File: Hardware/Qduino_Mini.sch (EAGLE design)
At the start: 44 parts, among them Q1 PFET, U1 ATMEGA32U41:1-LESS_PASTE, U2 MCP73831, U3 MAX17048, U4 TPS78233, U7 DNP, Y1 8MHZ

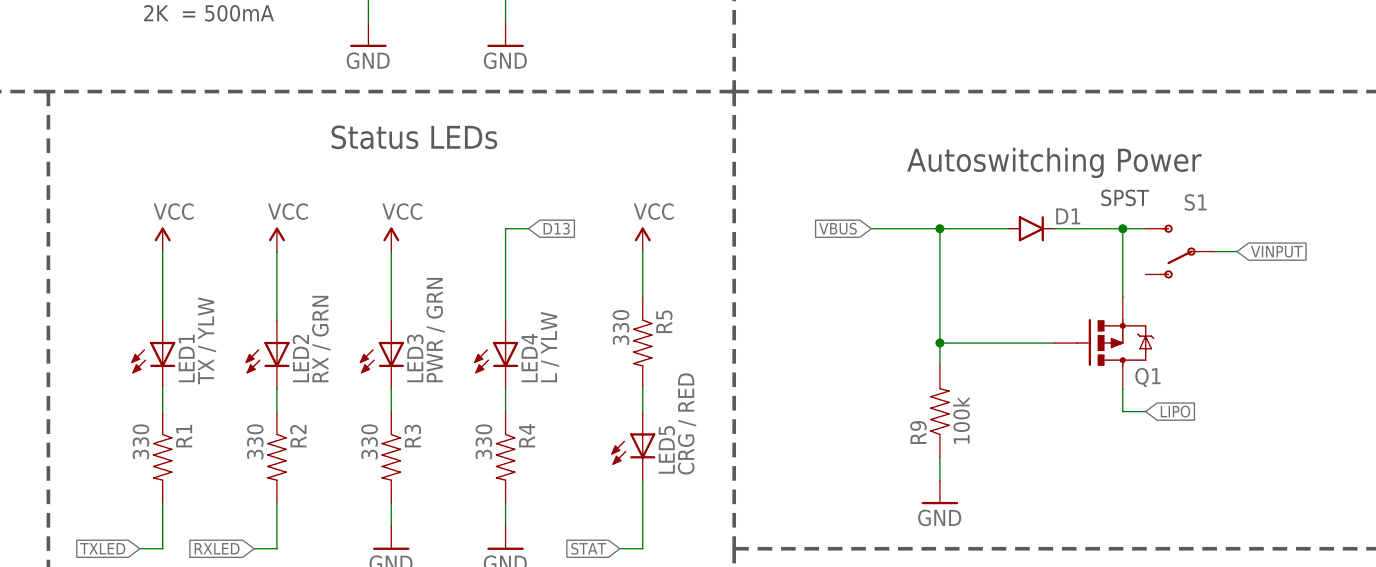
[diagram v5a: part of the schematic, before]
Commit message: Fixed library caused(?) inconsistencies
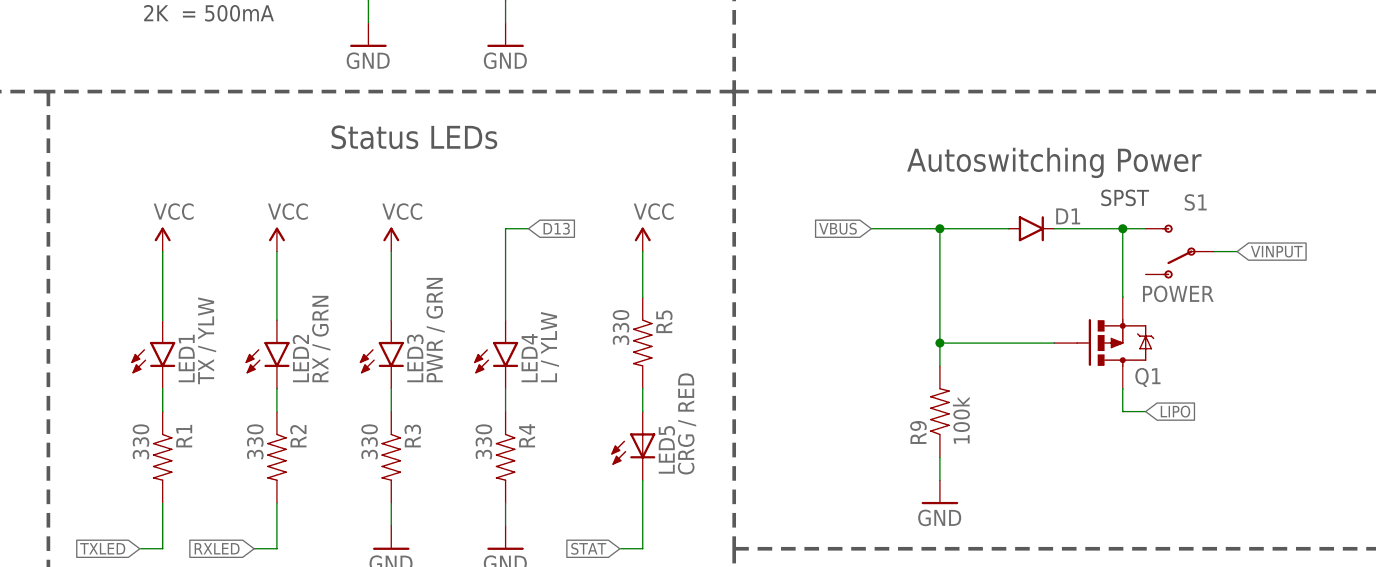
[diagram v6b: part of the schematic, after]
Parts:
- removed U$1: MIGHTYQ-S-SILK, Qtechknow:MIGHTYQ-S-SILK
- removed U$5: MIGHTYQ-L-SILK, Qtechknow:MIGHTYQ-L-SILK
- removed U$7, U$8, U$9: QHEADERS, Qtechknow:QHEADERS
- added U5: MIGHTYQ-L-SILK, SparkFun-Aesthetics:MIGHTYQ-L-SILK
- added U6: MIGHTYQ-S-SILK, SparkFun-Aesthetics:MIGHTYQ-S-SILK
- D1: value (none) -> BAS16JTR
- LED1, LED4: device SFE LED:LED0603 -> SparkFun-LED:LED-YELLOW0603
- LED2, LED3: device SFE LED:LED0603 -> SparkFun-LED:LED-GREEN0603
- S1: value (none) -> POWER
- U4: device Pinoccio:LDO-TPS78233 -> SparkFun-PowerIC:LDO-TPS78233
- U7: device Qduino_Mini:QDUINOMINI -> SparkFun-Aesthetics:QDUINOMINI
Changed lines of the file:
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@@
 <part name="GND2" library="SFE Aesthetics" deviceset="GND" device=""/>
 <part name="GND3" library="SFE Aesthetics" deviceset="GND" device=""/>
-<part name="LED1" library="SFE LED" deviceset="LED" device="0603" value="TX / YLW">
+<part name="LED1" library="SparkFun-LED" deviceset="LED-YELLOW" device="0603" value="TX / YLW">
 <attribute name="PROD_ID" value="DIO-09003"/>
 </part>
-<part name="LED2" library="SFE LED" deviceset="LED" device="0603" value="RX / GRN">
+<part name="LED2" library="SparkFun-LED" deviceset="LED-GREEN" device="0603" value="RX / GRN">
 <attribute name="PROD_ID" value="DIO-00821"/>
 </part>
 <part name="P+3" library="SFE Aesthetics" deviceset="VCC" device=""/>
-<part name="LED3" library="SFE LED" deviceset="LED" device="0603" value="PWR / GRN">
+<part name="LED3" library="SparkFun-LED" deviceset="LED-GREEN" device="0603" value="PWR / GRN">
 <attribute name="PROD_ID" value="DIO-00821"/>
 </part>
 <part name="P+4" library="SFE Aesthetics" deviceset="VCC" device=""/>
 <part name="GND6" library="SFE Aesthetics" deviceset="GND" device=""/>
-<part name="LED4" library="SFE LED" deviceset="LED" device="0603" value="L / YLW">
+<part name="LED4" library="SparkFun-LED" deviceset="LED-YELLOW" device="0603" value="L / YLW">
 <attribute name="PROD_ID" value="DIO-09003"/>
 </part>
@@
 <attribute name="PROD_ID" value="CAP-00868"/>
 </part>
-<part name="S1" library="SparkFun-Electromechanical" deviceset="SWITCH-SPDT" device="-SMD-A">
+<part name="S1" library="SparkFun-Electromechanical" deviceset="SWITCH-SPDT" device="-SMD-A" value="POWER">
 <attribute name="PROD_ID" value="SWCH-10651"/>
 </part>
@@
 <part name="GND16" library="SparkFun-Aesthetics" deviceset="GND" device=""/>
 <part name="GND15" library="SparkFun-Aesthetics" deviceset="GND" device=""/>
-<part name="U4" library="Pinoccio" deviceset="LDO-TPS78233" device="" value="TPS78233">
+<part name="U4" library="SparkFun-PowerIC" deviceset="LDO-TPS78233" device="" value="TPS78233">
 <attribute name="PROD_ID" value="12550"/>
 </part>
@@
 <part name="GND1" library="SparkFun" deviceset="GND" device=""/>
 <part name="GND9" library="SparkFun" deviceset="GND" device=""/>
-<part name="D1" library="SparkFun-DiscreteSemi" deviceset="DIODE" device="SOD"/>
-<part name="U$5" library="Qtechknow" deviceset="MIGHTYQ-L-SILK" device=""/>
-<part name="U$1" library="Qtechknow" deviceset="MIGHTYQ-S-SILK" device=""/>
+<part name="D1" library="SparkFun-DiscreteSemi" deviceset="DIODE" device="SOD" value="BAS16JTR"/>
+<part name="U5" library="SparkFun-Aesthetics" deviceset="MIGHTYQ-L-SILK" device=""/>
+<part name="U6" library="SparkFun-Aesthetics" deviceset="MIGHTYQ-S-SILK" device=""/>
 <part name="SJ1" library="SparkFun-Passives" deviceset="JUMPER-PAD-3-2OF3_NC_BY_PASTE" device="" value=""/>
 <part name="GND8" library="SparkFun" deviceset="GND" device=""/>
@@
 <attribute name="PROD_ID" value="RES-07857"/>
 </part>
-<part name="U7" library="Qduino_Mini" deviceset="QDUINOMINI" device="" value="DNP"/>
+<part name="U7" library="SparkFun-Aesthetics" deviceset="QDUINOMINI" device="" value="DNP"/>
 <part name="P+2" library="SFE Aesthetics" deviceset="VCC" device=""/>
 <part name="R12" library="SparkFun-Passives" deviceset="RESISTOR" device="0603-RES" value="4.7K">
@@
 <part name="Y1" library="SparkFun-FreqCtrl" deviceset="RESONATOR" device="8MHZ" value="8MHZ"/>
 <part name="GND22" library="SFE Aesthetics" deviceset="GND" device=""/>
-<part name="U$7" library="Qtechknow" deviceset="QHEADERS" device=""/>
-<part name="U$8" library="Qtechknow" deviceset="QHEADERS" device=""/>
-<part name="U$9" library="Qtechknow" deviceset="QHEADERS" device=""/>
 </parts>
 <sheets>
@@
 <instance part="GND1" gate="1" x="106.68" y="-5.08"/>
 <instance part="GND9" gate="1" x="114.3" y="-5.08"/>
-<instance part="D1" gate="G$1" x="121.92" y="63.5"/>
-<instance part="U$5" gate="G$1" x="83.82" y="-2.54"/>
-<instance part="U$1" gate="G$1" x="76.2" y="-2.54"/>
+<instance part="D1" gate="G$1" x="121.92" y="63.5" smashed="yes">
+<attribute name="NAME" x="124.46" y="63.9826" size="1.778" layer="95"/>
+</instance>
+<instance part="U5" gate="G$1" x="83.82" y="-2.54"/>
+<instance part="U6" gate="G$1" x="76.2" y="-2.54"/>
 <instance part="SJ1" gate="G$1" x="55.88" y="101.6" rot="R270"/>
 <instance part="GND8" gate="1" x="48.26" y="83.82"/>

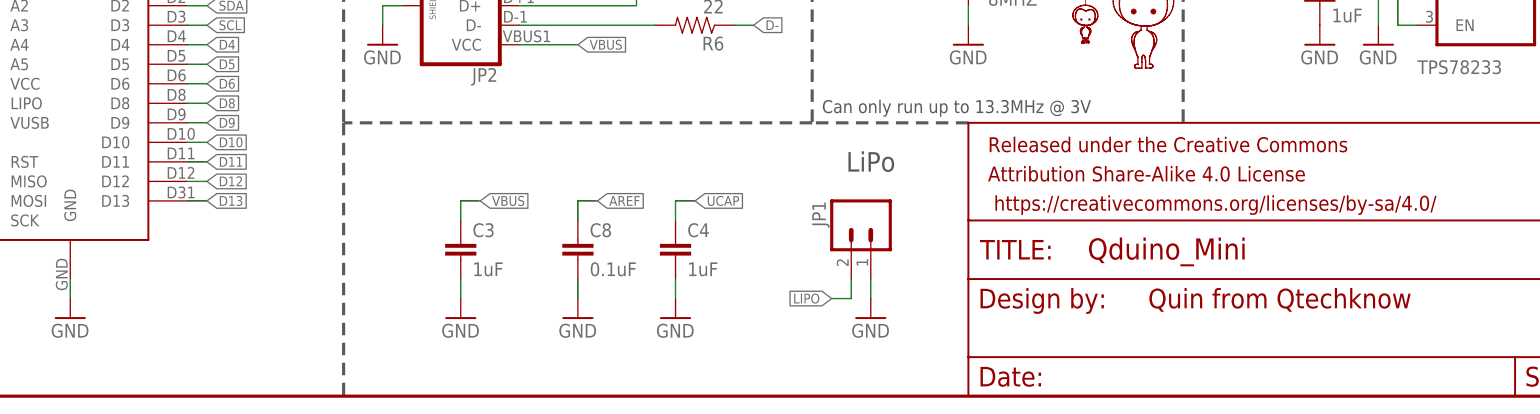
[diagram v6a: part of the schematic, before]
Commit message: Added logos to sch, massaged silk & a trace
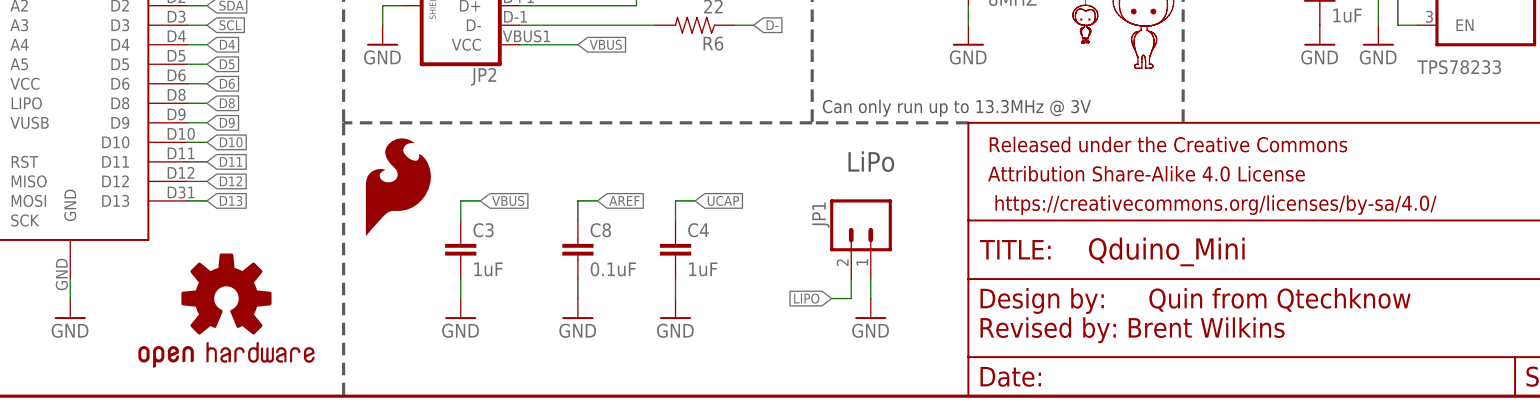
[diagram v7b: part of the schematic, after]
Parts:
- added LOGO1: OSHW-LOGOS, SparkFun-Aesthetics:OSHW-LOGOS
- added LOGO2: SFE_LOGO_FLAME.1_INCH, SparkFun-Aesthetics:SFE_LOGO_FLAME.1_INCH
- U3: device Pinoccio:MAX17048DFN8 -> SparkFun-DigitalIC:MAX17048DFN8
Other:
- note added: "Revised by: Brent Wilkins"
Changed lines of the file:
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@@
 <attribute name="PROD_ID" value="SWCH-10651"/>
 </part>
-<part name="U3" library="Pinoccio" deviceset="MAX17048" device="DFN8" value="MAX17048">
+<part name="U3" library="SparkFun-DigitalIC" deviceset="MAX17048" device="DFN8" value="MAX17048">
 <attribute name="PROD_ID" value="IC-12551"/>
 </part>
@@
 <part name="Y1" library="SparkFun-FreqCtrl" deviceset="RESONATOR" device="8MHZ" value="8MHZ"/>
 <part name="GND22" library="SFE Aesthetics" deviceset="GND" device=""/>
+<part name="LOGO1" library="SparkFun-Aesthetics" deviceset="OSHW-LOGO" device="S"/>
+<part name="LOGO2" library="SparkFun-Aesthetics" deviceset="SFE_LOGO_FLAME" device=".1_INCH"/>
 </parts>
 <sheets>
@@
 <wire x1="12.7" y1="78.74" x2="12.7" y2="20.32" width="0.4064" layer="97" style="shortdash"/>
 <text x="41.91" y="-13.97" size="1.6764" layer="97">Can only run up to 13.3MHz @ 3V</text>
+<text x="62.23" y="-43.18" size="2.54" layer="94" ratio="5">Revised by: Brent Wilkins</text>
 </plain>
 <instances>
@@
 <instance part="Y1" gate="G$1" x="60.96" y="7.62"/>
 <instance part="GND22" gate="1" x="60.96" y="-5.08"/>
+<instance part="LOGO1" gate="G$1" x="-35.56" y="-38.1"/>
+<instance part="LOGO2" gate="G$1" x="-17.78" y="-30.48"/>
 </instances>
 <busses>

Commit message: Complete rework
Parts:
- removed FID5, FID6: FIDUCIAL1X2, SparkFun-Aesthetics:FIDUCIAL1X2
- removed LED5: CRG / RED, SparkFun:LED0603
- removed R1, R3, R4: 330, SparkFun-Resistors:RESISTOR0603
- removed U6: MIGHTYQ-S-SILK, SparkFun-Aesthetics:MIGHTYQ-S-SILK
- removed U7: DNP, SparkFun-Aesthetics:QDUINOMINI
- added FID1, FID2: FIDUCIALUFIDUCIAL, SparkFun-Aesthetics:FIDUCIALUFIDUCIAL
- added JP3, JP4: (no value), SparkFun-Connectors:M12PTH
- D1: value BAS16JTR -> 250mA/100V; device SparkFun-DiscreteSemi:DIODESOD -> SparkFun-DiscreteSemi:DIODEBAS16
- JP2: value USB_MICROB_PLUGCONN-11752 -> (none)
- LED1: value TX / YLW -> RGB-LED-CLMVB-FKARGB; device SparkFun-LED:LED-YELLOW0603 -> Spark:RGB-LED-CLMVB-FKARGB; PROD_ID DIO-09003 -> (none)
- LED2: value RX / GRN -> RGB-LED-CLMVB-FKARGB; device SparkFun-LED:LED-GREEN0603 -> Spark:RGB-LED-CLMVB-FKARGB; PROD_ID DIO-00821 -> (none)
- R2, R5: device SparkFun-Resistors:RESISTOR0603 -> SparkFun-Passives:RESISTOR-ARRAY0603-ARV; PROD_ID RES-00818 -> (none)
- U4: value TPS78233 -> AP2112K-3.3TRG-1
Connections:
- removed net N$12: LED3.C, R3.1
- new net N$32: LED2.CBLUE, R5C.2
- new net N$34: LED1.CGREEN, R2B.2
- new net N$35: LED2.CRED, R5A.2
- new net N$37: LED2.CGREEN, R5B.2
- net A0: now also JP3.7; no longer U7.A0
- net A1: now also JP3.8; no longer U7.A1
- net A2: now also JP3.9; no longer U7.A2
- net A3: now also JP3.10; no longer U7.A3
- net A4: now also JP3.11; no longer U7.A4
- net A5: now also JP3.12; no longer U7.A5
- net D10: now also R5B.1; no longer U7.D10
- net D11: now also R5C.1; no longer U7.D11
- net D12: now also JP3.6; no longer U7.D12
- net D13: now also R5A.1; no longer LED4.A, U7.D13
- net D4: now also JP4.5; no longer U7.D4
- net D5: now also JP4.6; no longer U7.D5
- net D6: now also JP3.3; no longer U7.D6
- net D8: now also JP3.4; no longer U7.D8
- net D9: now also JP3.5; no longer U7.D9
- net GND: now also JP3.2, R2D.1, R5D.2; no longer R3.2, R4.2, U7.GND
- net LIPO: now also JP4.7; no longer U7.LIPO
- net MISO: now also JP4.10; no longer U7.MISO
- net MOSI: now also JP4.11; no longer U7.MOSI
- net N$1: now also LED1.CRED, R2A.2; no longer LED1.C, R1.1
- net N$2: now also LED1.CBLUE, R2C.2; no longer LED2.C, R2.1
- net N$4: now also LED3.C, R5D.1; no longer LED5.A, R5.2
- net N$5: now also R2D.2; no longer R4.1
- net RST: now also JP4.9; no longer U7.RST
- net RX: now also JP4.1; no longer U7.TX
- net RXLED: now also R2C.1, U1.PD5; no longer R2.2, U1.PB0(SS)
- net SCK: now also JP4.12, LED4.A; no longer U7.SCK
- net SCL: now also JP4.4; no longer U7.D3
- net SDA: now also JP4.3; no longer U7.D2
- net STAT: now also R2A.1; no longer LED5.C
- net TX: now also JP4.2; no longer U7.RX
- net TXLED: now also R2B.1, U1.PB0(SS); no longer R1.2, U1.PD5
- net VBUS: now also JP4.8; no longer U7.VUSB
- net VCC: now also JP3.1, LED1.A2, LED2.A2; no longer LED1.A, LED2.A, R5.1, U7.VCC
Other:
- note added: "3.3V @ 500mA max."
- note removed: "3.3V @ 150mA max."
- moved on the sheet: C5, C9, D1, JP2, LED3, LED4, Q1, R6, R7, R9, S1, U3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
